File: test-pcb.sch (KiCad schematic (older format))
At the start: 24 parts, among them SW1 SW_Push, U1 ATmega32U4-AU, Y1 16MHz

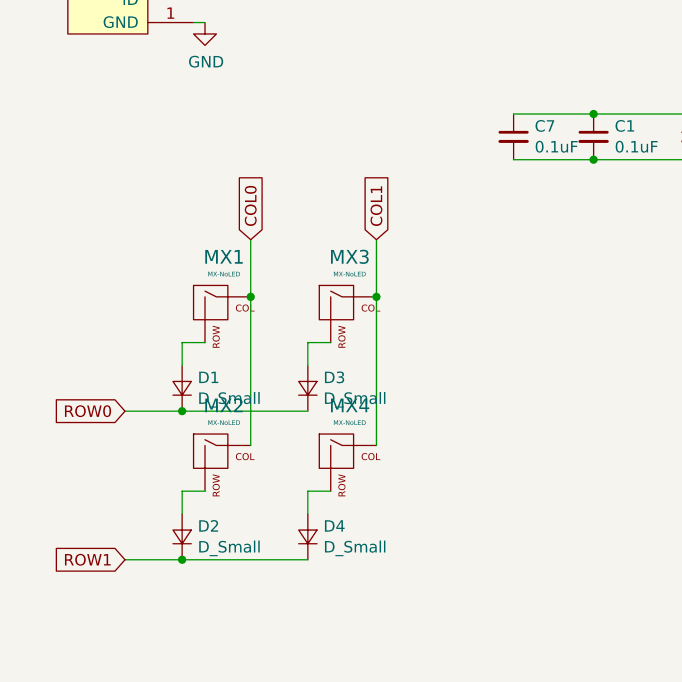
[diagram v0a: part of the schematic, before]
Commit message: added footprints
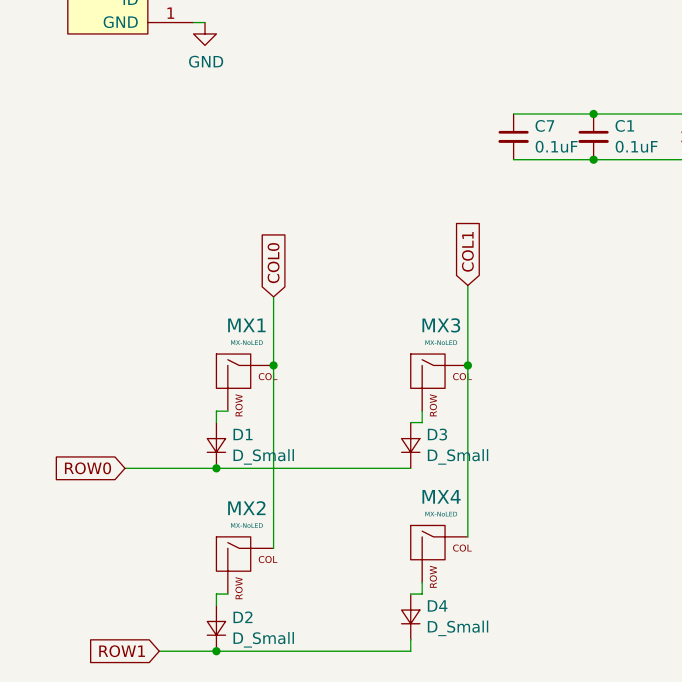
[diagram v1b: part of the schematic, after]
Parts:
- MX1, MX2, MX3, MX4: footprint (none) -> MX_Alps_Hybrid:MX-1U-NoLED
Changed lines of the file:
@@
 EESchema Schematic File Version 4
+LIBS:test-pcb-cache
 EELAYER 30 0
 EELAYER END
@@
 	1850 4000 1900 4000
 $Comp
-L MX_Alps_Hybrid:MX-NoLED MX1
-U 1 1 5F917685
-P 1950 5250
-F 0 "MX1" H 1983 5473 60  0000 C CNN
-F 1 "MX-NoLED" H 1983 5399 20  0000 C CNN
-F 2 "" H 1325 5225 60  0001 C CNN
-F 3 "" H 1325 5225 60  0001 C CNN
-	1    1950 5250
-	1    0    0    -1
-$EndComp
-$Comp
-L Device:D_Small D1
-U 1 1 5F918584
-P 1800 5600
-F 0 "D1" V 1846 5532 50  0000 R CNN
-F 1 "D_Small" V 1755 5532 50  0000 R CNN
-F 2 "Diode_SMD:D_SOD-123" V 1800 5600 50  0001 C CNN
-F 3 "~" V 1800 5600 50  0001 C CNN
-	1    1800 5600
-	0    -1   -1   0
-$EndComp
-Wire Wire Line
-	1900 5400 1800 5400
-Wire Wire Line
-	1800 5400 1800 5500
-$Comp
-L MX_Alps_Hybrid:MX-NoLED MX3
-U 1 1 5F91B66A
-P 2500 5250
-F 0 "MX3" H 2533 5473 60  0000 C CNN
-F 1 "MX-NoLED" H 2533 5399 20  0000 C CNN
-F 2 "" H 1875 5225 60  0001 C CNN
-F 3 "" H 1875 5225 60  0001 C CNN
-	1    2500 5250
-	1    0    0    -1
-$EndComp
-$Comp
-L MX_Alps_Hybrid:MX-NoLED MX4
-U 1 1 5F91C5C5
-P 2500 5900
-F 0 "MX4" H 2533 6123 60  0000 C CNN
-F 1 "MX-NoLED" H 2533 6049 20  0000 C CNN
-F 2 "" H 1875 5875 60  0001 C CNN
-F 3 "" H 1875 5875 60  0001 C CNN
-	1    2500 5900
-	1    0    0    -1
-$EndComp
-$Comp
-L MX_Alps_Hybrid:MX-NoLED MX2
-U 1 1 5F91D607
-P 1950 5900
-F 0 "MX2" H 1983 6123 60  0000 C CNN
-F 1 "MX-NoLED" H 1983 6049 20  0000 C CNN
-F 2 "" H 1325 5875 60  0001 C CNN
-F 3 "" H 1325 5875 60  0001 C CNN
-	1    1950 5900
-	1    0    0    -1
-$EndComp
-$Comp
-L Device:D_Small D3
-U 1 1 5F91E0CB
-P 2350 5600
-F 0 "D3" V 2396 5532 50  0000 R CNN
-F 1 "D_Small" V 2305 5532 50  0000 R CNN
-F 2 "Diode_SMD:D_SOD-123" V 2350 5600 50  0001 C CNN
-F 3 "~" V 2350 5600 50  0001 C CNN
-	1    2350 5600
-	0    -1   -1   0
-$EndComp
-$Comp
-L Device:D_Small D4
-U 1 1 5F91EF7C
-P 2350 6250
-F 0 "D4" V 2396 6182 50  0000 R CNN
-F 1 "D_Small" V 2305 6182 50  0000 R CNN
-F 2 "Diode_SMD:D_SOD-123" V 2350 6250 50  0001 C CNN
-F 3 "~" V 2350 6250 50  0001 C CNN
-	1    2350 6250
-	0    -1   -1   0
-$EndComp
-$Comp
-L Device:D_Small D2
-U 1 1 5F920067
-P 1800 6250
-F 0 "D2" V 1846 6182 50  0000 R CNN
-F 1 "D_Small" V 1755 6182 50  0000 R CNN
-F 2 "Diode_SMD:D_SOD-123" V 1800 6250 50  0001 C CNN
-F 3 "~" V 1800 6250 50  0001 C CNN
-	1    1800 6250
-	0    -1   -1   0
-$EndComp
-Wire Wire Line
-	2450 5400 2350 5400
-Wire Wire Line
-	2350 5400 2350 5500
-Wire Wire Line
-	2450 6050 2350 6050
-Wire Wire Line
-	2350 6050 2350 6150
-Wire Wire Line
-	1900 6050 1800 6050
-Wire Wire Line
-	1800 6050 1800 6150
-Wire Wire Line
-	2350 5700 1800 5700
-Wire Wire Line
-	1800 5700 1550 5700
-Connection ~ 1800 5700
-Wire Wire Line
-	2350 6350 1800 6350
-Connection ~ 1800 6350
-Wire Wire Line
-	1800 6350 1550 6350
-Wire Wire Line
-	2100 5850 2100 5200
-Connection ~ 2100 5200
-Wire Wire Line
-	2650 5850 2650 5200
-Connection ~ 2650 5200
-Text GLabel 2100 4950 1    50   Input ~ 0
-COL0
-Text GLabel 2650 4950 1    50   Input ~ 0
-COL1
-Wire Wire Line
-	2100 4950 2100 5200
-Wire Wire Line
-	2650 4950 2650 5200
-Text GLabel 1550 5700 0    50   Input ~ 0
-ROW0
-Text GLabel 1550 6350 0    50   Input ~ 0
-ROW1
-$Comp
 L Device:C_Small C7
 U 1 1 5F92F81F
@@
 	3250 4600 3600 4600
 Connection ~ 3600 4600
+$Comp
+L MX_Alps_Hybrid:MX-NoLED MX1
+U 1 1 5F8DCB33
+P 2050 5550
+F 0 "MX1" H 2083 5773 60  0000 C CNN
+F 1 "MX-NoLED" H 2083 5699 20  0000 C CNN
+F 2 "MX_Alps_Hybrid:MX-1U-NoLED" H 1425 5525 60  0001 C CNN
+F 3 "" H 1425 5525 60  0001 C CNN
+	1    2050 5550
+	1    0    0    -1
+$EndComp
+$Comp
+L MX_Alps_Hybrid:MX-NoLED MX3
+U 1 1 5F8DDC7A
+P 2900 5550
+F 0 "MX3" H 2933 5773 60  0000 C CNN
+F 1 "MX-NoLED" H 2933 5699 20  0000 C CNN
+F 2 "MX_Alps_Hybrid:MX-1U-NoLED" H 2275 5525 60  0001 C CNN
+F 3 "" H 2275 5525 60  0001 C CNN
+	1    2900 5550
+	1    0    0    -1
+$EndComp
+$Comp
+L MX_Alps_Hybrid:MX-NoLED MX4
+U 1 1 5F8DEAF5
+P 2900 6300
+F 0 "MX4" H 2933 6523 60  0000 C CNN
+F 1 "MX-NoLED" H 2933 6449 20  0000 C CNN
+F 2 "MX_Alps_Hybrid:MX-1U-NoLED" H 2275 6275 60  0001 C CNN
+F 3 "" H 2275 6275 60  0001 C CNN
+	1    2900 6300
+	1    0    0    -1
+$EndComp
+$Comp
+L MX_Alps_Hybrid:MX-NoLED MX2
+U 1 1 5F8DFEB3
+P 2050 6350
+F 0 "MX2" H 2083 6573 60  0000 C CNN
+F 1 "MX-NoLED" H 2083 6499 20  0000 C CNN
+F 2 "MX_Alps_Hybrid:MX-1U-NoLED" H 1425 6325 60  0001 C CNN
+F 3 "" H 1425 6325 60  0001 C CNN
+	1    2050 6350
+	1    0    0    -1
+$EndComp
+$Comp
+L Device:D_Small D1
+U 1 1 5F8E0962
+P 1950 5850
+F 0 "D1" V 1996 5782 50  0000 R CNN
+F 1 "D_Small" V 1905 5782 50  0000 R CNN
+F 2 "Diode_SMD:D_SOD-123" V 1950 5850 50  0001 C CNN
+F 3 "~" V 1950 5850 50  0001 C CNN
+	1    1950 5850
+	0    -1   -1   0
+$EndComp
+$Comp
+L Device:D_Small D3
+U 1 1 5F8E16BC
+P 2800 5850
+F 0 "D3" V 2846 5782 50  0000 R CNN
+F 1 "D_Small" V 2755 5782 50  0000 R CNN
+F 2 "Diode_SMD:D_SOD-123" V 2800 5850 50  0001 C CNN
+F 3 "~" V 2800 5850 50  0001 C CNN
+	1    2800 5850
+	0    -1   -1   0
+$EndComp
+$Comp
+L Device:D_Small D4
+U 1 1 5F8E218F
+P 2800 6600
+F 0 "D4" V 2846 6532 50  0000 R CNN
+F 1 "D_Small" V 2755 6532 50  0000 R CNN
+F 2 "Diode_SMD:D_SOD-123" V 2800 6600 50  0001 C CNN
+F 3 "~" V 2800 6600 50  0001 C CNN
+	1    2800 6600
+	0    -1   -1   0
+$EndComp
+$Comp
+L Device:D_Small D2
+U 1 1 5F8E2D75
+P 1950 6650
+F 0 "D2" V 1996 6582 50  0000 R CNN
+F 1 "D_Small" V 1905 6582 50  0000 R CNN
+F 2 "Diode_SMD:D_SOD-123" V 1950 6650 50  0001 C CNN
+F 3 "~" V 1950 6650 50  0001 C CNN
+	1    1950 6650
+	0    -1   -1   0
+$EndComp
+Wire Wire Line
+	2000 5700 1950 5700
+Wire Wire Line
+	1950 5700 1950 5750
+Wire Wire Line
+	2000 6500 1950 6500
+Wire Wire Line
+	1950 6500 1950 6550
+Wire Wire Line
+	2800 6500 2850 6500
+Wire Wire Line
+	2850 6500 2850 6450
+Wire Wire Line
+	2800 5750 2850 5750
+Wire Wire Line
+	2850 5750 2850 5700
+Wire Wire Line
+	1550 5950 1950 5950
+Connection ~ 1950 5950
+Wire Wire Line
+	1950 5950 2800 5950
+Wire Wire Line
+	2800 6700 2800 6750
+Wire Wire Line
+	2800 6750 1950 6750
+Connection ~ 1950 6750
+Wire Wire Line
+	1950 6750 1700 6750
+Wire Wire Line
+	2200 6300 2200 5500
+Wire Wire Line
+	3050 5500 3050 6250
+Text GLabel 1550 5950 0    50   Input ~ 0
+ROW0
+Text GLabel 1700 6750 0    50   Input ~ 0
+ROW1
+Text GLabel 2200 5200 1    50   Input ~ 0
+COL0
+Text GLabel 3050 5150 1    50   Input ~ 0
+COL1
+Wire Wire Line
+	2200 5500 2200 5200
+Connection ~ 2200 5500
+Wire Wire Line
+	3050 5150 3050 5500
+Connection ~ 3050 5500
 $EndSCHEMATC

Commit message: gerbers!
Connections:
- net COL0: now also U1.29 (PB5)
- net COL1: now also U1.28 (PB4)
- net GND: now also Y1.2, Y1.4
- net ROW0: now also U1.27 (PD7)
- net ROW1: now also U1.30 (PB6)
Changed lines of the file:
@@
 Connection ~ 3950 2700
-Wire Wire Line
-	4000 2850 4400 2850
 Wire Wire Line
 	4400 2850 4400 2750
@@
 	3050 5150 3050 5500
 Connection ~ 3050 5500
+Wire Wire Line
+	3950 2850 4400 2850
+Connection ~ 3950 2850
+Text GLabel 6150 2700 2    50   Input ~ 0
+COL0
+Text GLabel 6150 2600 2    50   Input ~ 0
+COL1
+Text GLabel 6150 2800 2    50   Input ~ 0
+ROW1
+Text GLabel 6150 4100 2    50   Input ~ 0
+ROW0
 $EndSCHEMATC
